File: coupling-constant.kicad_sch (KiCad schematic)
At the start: 33 parts, among them J1 Input, J102 Output, J104 DC IN, U101 TL072, U102 TC1044SxOA

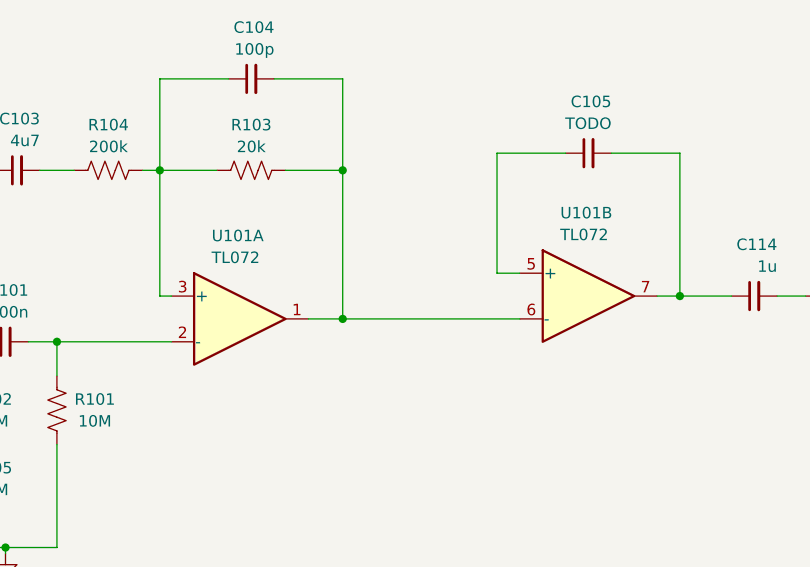
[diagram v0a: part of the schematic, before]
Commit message: v1, fixup op amp inputs
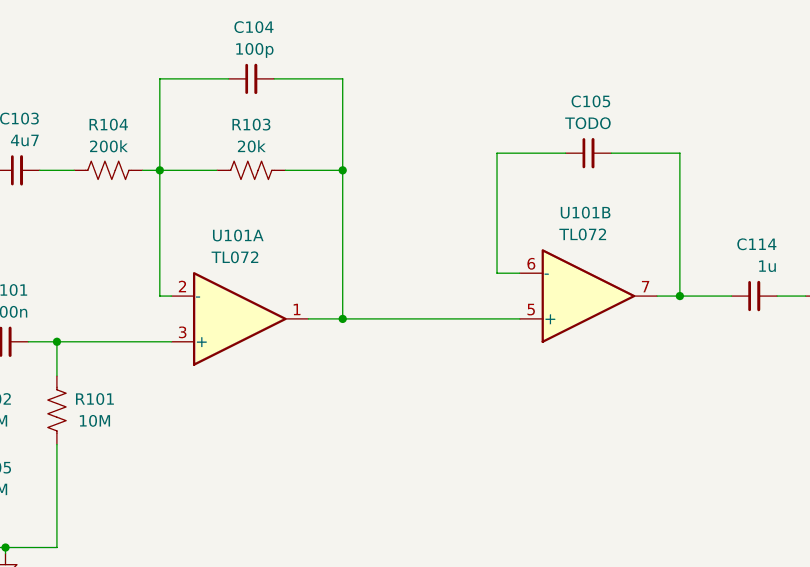
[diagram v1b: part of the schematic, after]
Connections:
- net at C104.1, R103.1, R104.2: now also U101.2 (-); no longer U101.3 (+)
- net at C104.2, R103.2, U101.1: now also U101.5 (+); no longer U101.6 (-)
- net at C105.1: now also U101.6 (-); no longer U101.5 (+)
- net at C101.2, R101.1: now also U101.3 (+); no longer U101.2 (-)
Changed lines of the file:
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@@
   (title_block
     (title "Coupling Constant")
-    (date "2024-01-07")
-    (rev "v0")
+    (date "2024-01-20")
+    (rev "v1")
     (company "Winterbloom")
     (comment 1 "Alethea Flowers")
@@
     )
   )
-  (symbol (lib_id "Amplifier_Operational:TL072") (at 128.905 84.455 0) (unit 1)
+  (symbol (lib_id "Amplifier_Operational:TL072") (at 128.905 84.455 0) (mirror x) (unit 1)
     (in_bom yes) (on_board yes) (dnp no) (fields_autoplaced)
     (property "Reference" "U101" (at 125.77 75.2307 0)
@@
     )
   )
-  (symbol (lib_id "Amplifier_Operational:TL072") (at 167.64 81.915 0) (unit 2)
-    (in_bom yes) (on_board yes) (dnp no) (fields_autoplaced)
-    (property "Reference" "U101" (at 164.505 72.6907 0)
-      (effects (font (size 1.27 1.27)) (justify left))
-    )
-    (property "Value" "TL072" (at 164.505 75.1149 0)
-      (effects (font (size 1.27 1.27)) (justify left))
-    )
+  (symbol (lib_id "Amplifier_Operational:TL072") (at 167.64 81.915 0) (mirror x) (unit 2)
+    (in_bom yes) (on_board yes) (dnp no) (fields_autoplaced)
+    (property "Reference" "U101" (at 164.4143 72.6907 0)
+      (effects (font (size 1.27 1.27)) (justify left))
+    )
+    (property "Value" "TL072" (at 164.4143 75.1149 0)
+      (effects (font (size 1.27 1.27)) (justify left))
+    )

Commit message: finalize v1
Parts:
- added D6: Power, LED_THT:LED_D3.0mm, symbol Device:LED_Small_Filled
- added R8: 4k7, winterbloom:R_0805_HandSolder, symbol Device:R_US
- C10: renamed from C104; footprint winterbloom:R_0805_HandSolder -> winterbloom:C_0805_HandSolder
- C13: renamed from C105; footprint winterbloom:R_0805_HandSolder -> winterbloom:C_0805_HandSolder
- C9: renamed from C103; footprint winterbloom:R_0805_HandSolder -> winterbloom:C_0805_HandSolder
- R6: renamed from R109; footprint winterbloom:C_0805_HandSolder -> winterbloom:R_0805_HandSolder
- U2: renamed from U101; footprint Package_SO:TSSOP-8_4.4x3mm_P0.65mm -> Package_SO:SOIC-8_3.9x4.9mm_P1.27mm; mpn TL072CPWR -> (none)
- renumbered C102 to C1, C113 to C11, C106 to C12, C114 to C14, C108 to C2, C111 to C3, C109 to C4, C110 to C5, C107 to C6, C112 to C7, C101 to C8, D101 to D1, D105 to D2, D103 to D3, D107 to D4, D106 to D5, J104 to J1, J1 to J2, J102 to J3, R101 to R1, R105 to R2, R102 to R3, R104 to R4, R103 to R5, R108 to R7, TP102 to TP1, TP103 to TP2, U102 to U1
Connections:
- net +9V: now also R8.2
- net GND: now also D6.1 (K)
- net at C10.1, R4.2, R5.1: now also U2.6 (-); no longer U2.2 (-)
- net at C10.2, R5.2: now also U2.3 (+), U2.7; no longer U2.1, U2.5 (+)
- net at C13.1: now also U2.2 (-); no longer U2.6 (-)
- net at C13.2, C14.1: now also U2.1; no longer U2.7
- net at C8.2, R1.1: now also U2.5 (+); no longer U2.3 (+)
- new net: D6.2 (A), R8.1
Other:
- note added: "Power: - VCC = (Vin * 2) - (Vf * 2) - VCC = (9 V * 2) - (0.45 V * 2) - VCC = +17 V - VEE = -(9 V * 2) - (0.45 V * 2) - VEE = -17V Input voltage: - Single coil: ~100mV pkpk max - Humbucker: ~500mV pkpk max Input Impedance: - R1 || (R3 + R2) = ~7MΩ Input high-pass filter: * R1 & C8 = 0.2 Hz Amplifier frequency response: * Low-pass filter R5 & C10 = 79kHz * High-pass filter R4 & C9 = 1.6 Hz Gain: * 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"
- note removed: "Input voltage: * Single coil: ~100mV pkpk max * Humbucker: ~500mV pkpk max Input Impedance: * R101 || R102 = ~7MΩ Input high-pass filter: * R101 & C101 = 0.2 Hz Amplifier frequency response: * Low-pass filter R103 & C104 = 79kHz * High-pass filter R104 & C103 = 1.6 Hz Gain: * 1 + (R103 / R104) = 1.1 Output: - High-pass filter C114 & R108 = 0.01 Hz"
- note removed: "VCC = (Vin * 2) - (Vf * 2) VCC = (9 V * 2) - (0.45 V * 2) VCC = +17 V VSS = -(9 V * 2) - (0.45 V * 2) VSS = -17V"
- moved on the sheet: C1, D1, J1
